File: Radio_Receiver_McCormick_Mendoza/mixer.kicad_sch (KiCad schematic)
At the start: 20 parts, among them J13 I_0, J14 I_180, J15 Q_90, J16 Q_270, J17 I_OUT, J18 Conn_01x02_Female, J19 Conn_01x02_Female, J20 Q_OUT, U11 INA821ID, U8 SN74CBT3253CDBR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

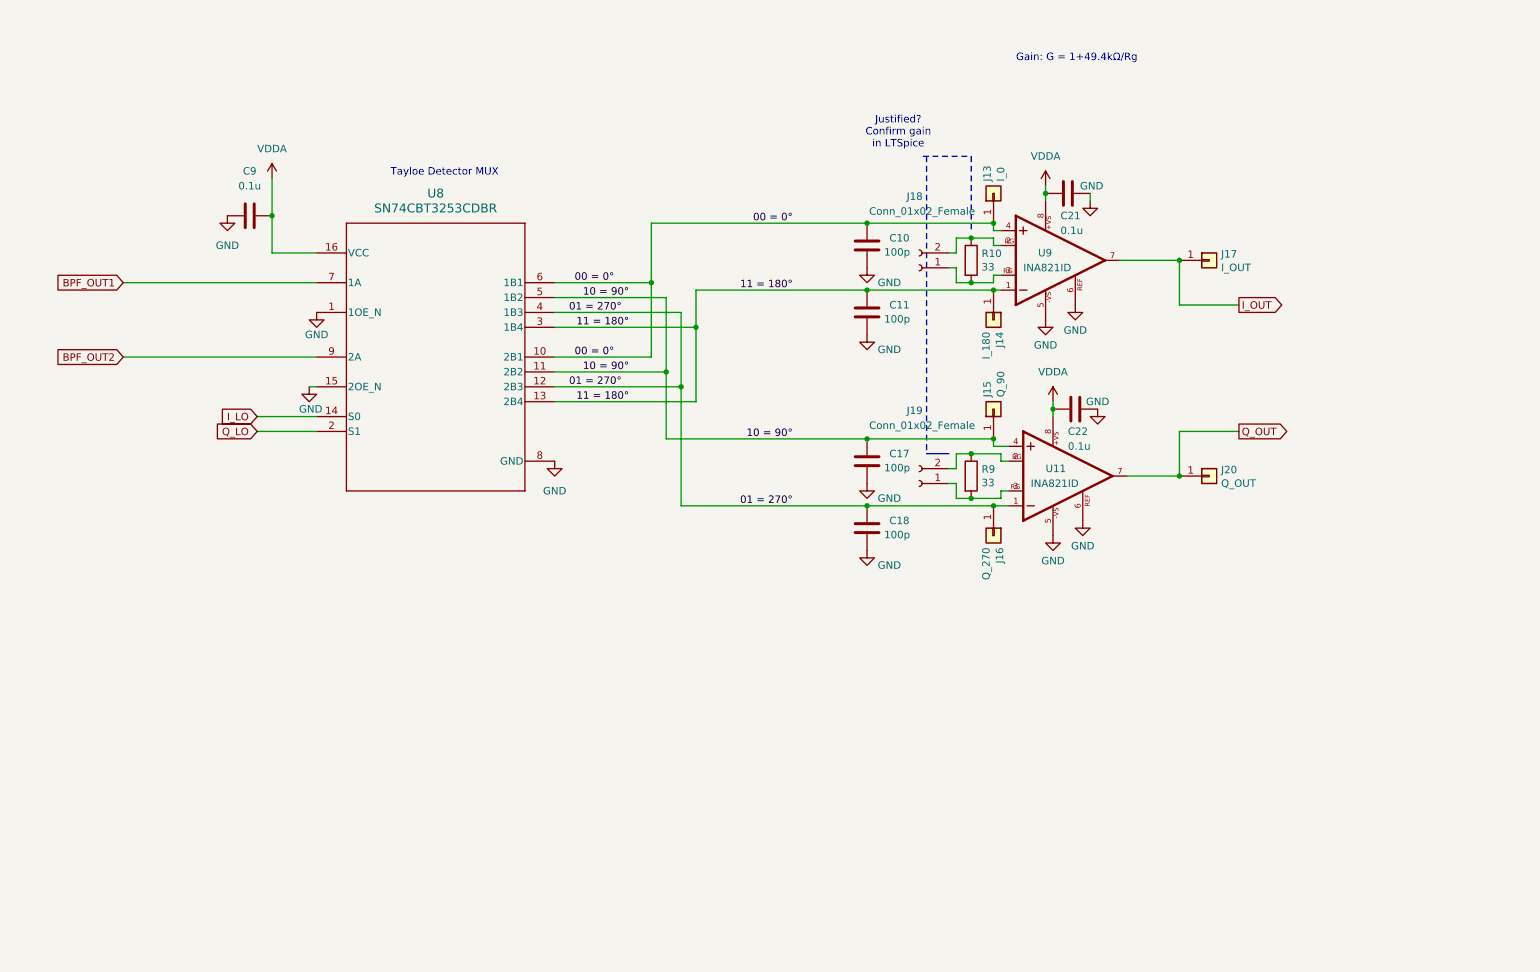
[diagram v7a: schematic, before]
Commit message: Added reference voltage stability by buffer amp
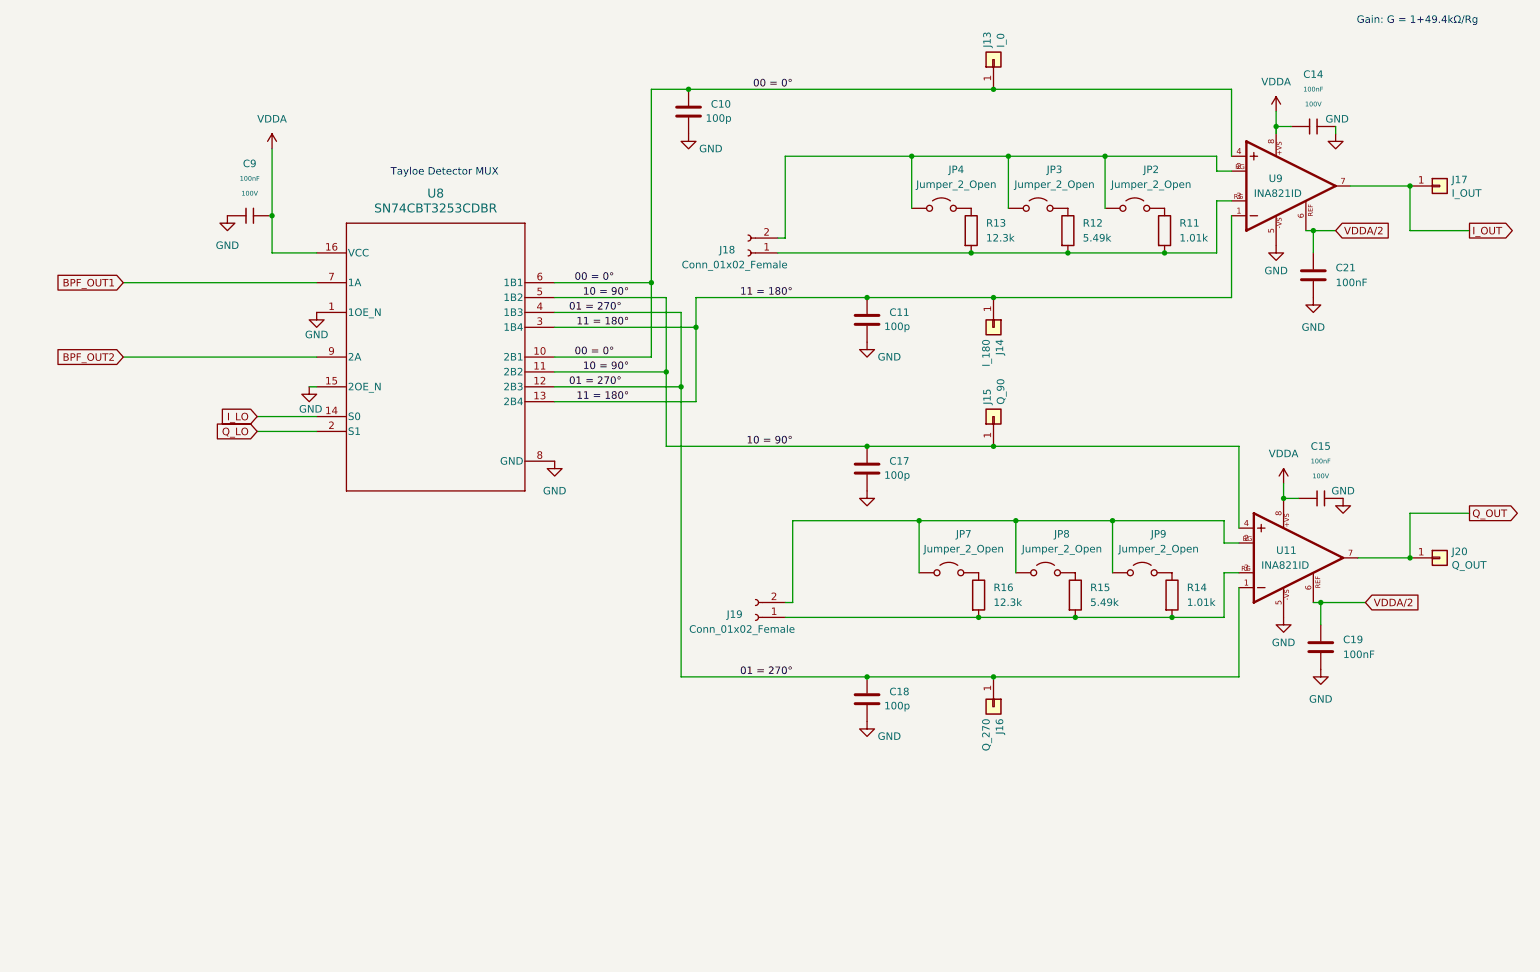
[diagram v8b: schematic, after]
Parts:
- removed C22, C9: 0.1u, Capacitor_THT:C_Disc_D5.1mm_W3.2mm_P5.00mm, symbol Device:C
- removed R10, R9: 33, Resistor_THT:R_Axial_DIN0207_L6.3mm_D2.5mm_P7.62mm_Horizontal, symbol Device:R
- added C14, C15, C9: 100nF, PCM_JLCPCB:C_0805, symbol PCM_JLCPCB-Capacitors:0805,100nF
- added C19: 100nF, PCM_JLCPCB:C_1206, symbol Device:C
- added JP2, JP3, JP4, JP7, JP8, JP9: Jumper_2_Open, symbol Jumper:Jumper_2_Open
- added R11, R14: 1.01k, PCM_JLCPCB:R_0603, symbol Device:R
- added R12, R15: 5.49k, PCM_JLCPCB:R_0603, symbol Device:R
- added R13, R16: 12.3k, PCM_JLCPCB:R_0603, symbol Device:R
- C21: value 0.1u -> 100nF; footprint Capacitor_THT:C_Disc_D5.1mm_W3.2mm_P5.00mm -> PCM_JLCPCB:C_1206
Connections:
- net GND: now also C21.2, C14.2, C15.2, C19.2, C9.1; no longer C21.1, U11.6 (REF), U9.6 (REF)
- net VDDA: now also C14.1, C15.1, C9.2; no longer C21.2
- net at J19.1 (Pin_1), U11.3 (RG1): now also R14.2, R15.2, R16.2
- net at J19.2 (Pin_2), U11.2 (RG): now also JP7.1 (A), JP8.1 (A), JP9.1 (A)
- net at J18.2 (Pin_2), U9.2 (RG): now also JP2.1 (A), JP3.1 (A), JP4.1 (A)
- net at J18.1 (Pin_1), U9.3 (RG1): now also R11.2, R12.2, R13.2
- new net: JP7.2 (B), R16.1
- new net: JP3.2 (B), R12.1
- new net: JP9.2 (B), R14.1
- new net: JP2.2 (B), R11.1
- new net: JP8.2 (B), R15.1
- new net: JP4.2 (B), R13.1
- new net VDDA/2: C19.1, C21.1, U11.6 (REF), U9.6 (REF)
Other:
- note removed: "Justified? Confirm gain in LTSpice"
- moved on the sheet: C10, C11, C17, C18, J13, J14, J15, J16, J17, J18, J20, U11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
